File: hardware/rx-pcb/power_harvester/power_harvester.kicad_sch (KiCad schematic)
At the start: 47 parts, among them J1 Conn_Coaxial_Small, J2 Conn_01x02_Pin, J3 Conn_Coaxial_Small, J4 Conn_Coaxial_Small

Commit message: updates for dr weeks
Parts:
- C8: footprint (none) -> Capacitor_SMD:C_0805_2012Metric_Pad1.18x1.45mm_HandSolder
- J3, J4: footprint Connector_PinHeader_2.54mm:PinHeader_1x02_P2.54mm_Vertical -> Connector_Coaxial:SMA_Molex_73251-2120_EdgeMount_Horizontal
- L1, L3: footprint Inductor_SMD:L_0805_2012Metric_Pad1.05x1.20mm_HandSolder -> Inductor_SMD:L_0402_1005Metric
- R12, R13, R8: value off -> on
- R2: value on -> off
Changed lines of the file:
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@@
 			)
 		)
-		(property "Footprint" "Inductor_SMD:L_0805_2012Metric_Pad1.05x1.20mm_HandSolder"
+		(property "Footprint" "Inductor_SMD:L_0402_1005Metric"
 			(at 58.42 43.18 0)
 			(hide yes)
@@
 			)
 		)
-		(property "Value" "off"
+		(property "Value" "on"
 			(at 49.276 120.904 90)
 			(show_name no)
@@
 			)
 		)
-		(property "Footprint" ""
+		(property "Footprint" "Capacitor_SMD:C_0805_2012Metric_Pad1.18x1.45mm_HandSolder"
 			(at 164.1348 49.53 0)
 			(hide yes)
@@
 			)
 		)
-		(property "Footprint" "Inductor_SMD:L_0805_2012Metric_Pad1.05x1.20mm_HandSolder"
+		(property "Footprint" "Inductor_SMD:L_0402_1005Metric"
 			(at 58.42 48.26 0)
 			(hide yes)
@@
 			)
 		)
-		(property "Value" "off"
+		(property "Value" "on"
 			(at 63.246 120.904 90)
 			(show_name no)
@@
 			)
 		)
-		(property "Value" "on"
+		(property "Value" "off"
 			(at 68.326 120.904 90)
 			(show_name no)
@@
 			)
 		)
-		(property "Footprint" "Connector_PinHeader_2.54mm:PinHeader_1x02_P2.54mm_Vertical"
+		(property "Footprint" "Connector_Coaxial:SMA_Molex_73251-2120_EdgeMount_Horizontal"
 			(at 184.15 33.02 0)
 			(hide yes)
@@
 			)
 		)
-		(property "Footprint" "Connector_PinHeader_2.54mm:PinHeader_1x02_P2.54mm_Vertical"
+		(property "Footprint" "Connector_Coaxial:SMA_Molex_73251-2120_EdgeMount_Horizontal"
 			(at 123.19 33.02 0)
 			(hide yes)
@@
 			)
 		)
-		(property "Value" "off"
+		(property "Value" "on"
 			(at 65.786 120.904 90)
 			(show_name no)

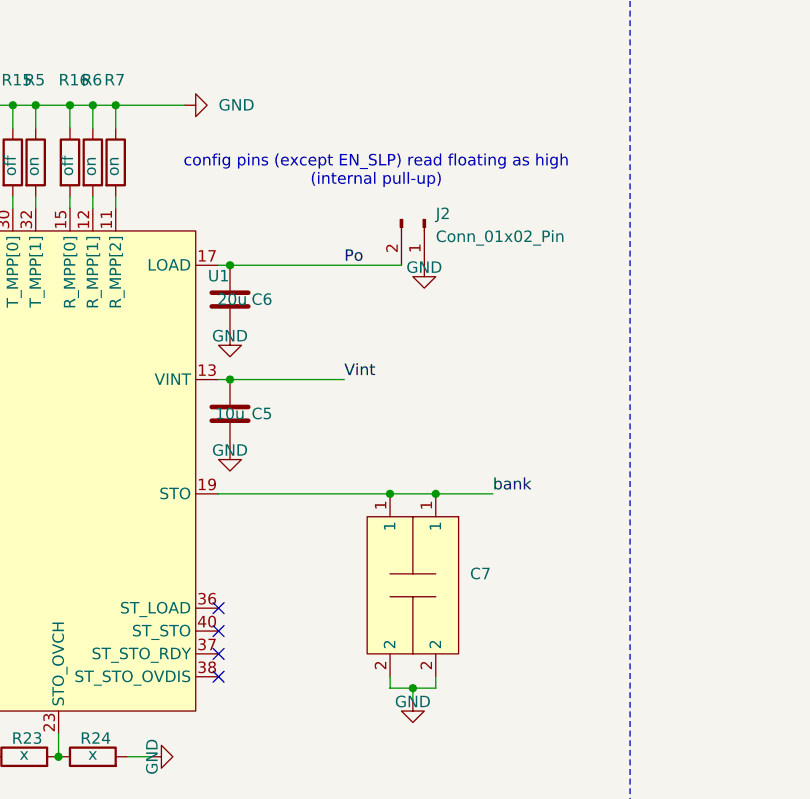
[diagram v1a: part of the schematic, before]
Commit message: updated PCB for weeks purchase
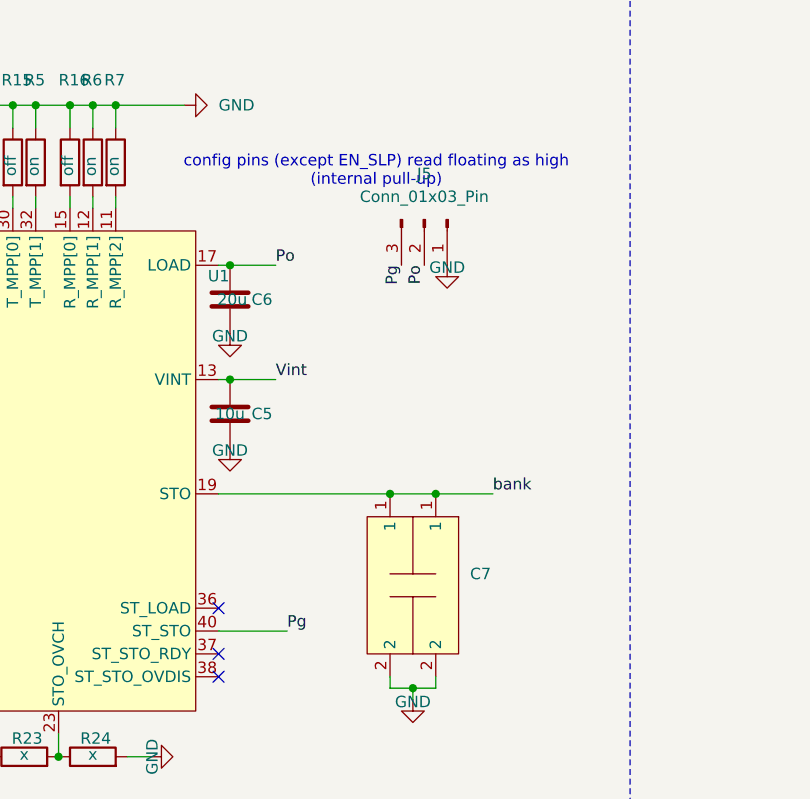
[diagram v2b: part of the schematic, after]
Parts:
- removed J2: Conn_01x02_Pin, Connector_PinHeader_2.54mm:PinHeader_1x02_P2.54mm_Vertical, symbol Connector:Conn_01x02_Pin
- added J5: Conn_01x03_Pin, Connector_PinHeader_2.54mm:PinHeader_1x03_P2.54mm_Vertical, symbol Connector:Conn_01x03_Pin
- D1, D2: footprint power_harvester:JDH2S02SL -> power_harvester:R_0201_0603Metric_correctedclearance
- D3, D4: footprint Capacitor_SMD:C_0201_0603Metric -> power_harvester:R_0201_0603Metric_correctedclearance
- R1, R10, R11, R12, R13, R14, R15, R16, R2, R3, R4, R5, R6, R7, R8, R9: footprint Resistor_SMD:R_0201_0603Metric -> power_harvester:R_0201_0603Metric_correctedclearance
- R17, R18, R19, R20: footprint Resistor_SMD:R_0201_0603Metric_Pad0.64x0.40mm_HandSolder -> power_harvester:R_0201_0603Metric_correctedclearance
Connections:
- net GND: now also J5.1 (Pin_1)
- net Po: now also J5.2 (Pin_2)
- net Pg: now reaches U1.40 (ST_STO)
- net Pg: now also J5.3 (Pin_3)
- no-connect marks 4 -> 3

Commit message: minor harvester updates
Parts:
- R12, R13, R4: value on -> off
- R14: value off -> on
- R21: value x -> 0
- R22: value x -> 19.5M
- R23: value x -> 100k
- R24: value x -> 5.6M
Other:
- note added: "R4 R3 R2 R1"
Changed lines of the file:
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@@
 		)
 	)
+	(text "R4     R3     R2     R1"
+		(exclude_from_sim no)
+		(at 78.74 188.468 0)
+		(effects
+			(font
+				(size 1.27 1.27)
+			)
+		)
+	)
 	(text "config pins (except EN_SLP) read floating as high\n(internal pull-up)"
 		(exclude_from_sim no)
@@
 			)
 		)
-		(property "Value" "x"
-			(at 75.438 185.166 90)
+		(property "Value" "19.5M"
+			(at 77.978 190.246 90)
 			(show_name no)
 			(do_not_autoplace no)
@@
 			)
 		)
-		(property "Value" "x"
-			(at 90.678 185.166 90)
+		(property "Value" "5.6M"
+			(at 91.948 190.246 90)
 			(show_name no)
 			(do_not_autoplace no)
@@
 			)
 		)
-		(property "Value" "x"
-			(at 83.058 185.166 90)
+		(property "Value" "100k"
+			(at 85.09 190.246 90)
 			(show_name no)
 			(do_not_autoplace no)
@@
 			)
 		)
-		(property "Value" "on"
+		(property "Value" "off"
 			(at 77.216 120.904 90)
 			(show_name no)
@@
 			)
 		)
-		(property "Value" "off"
+		(property "Value" "on"
 			(at 74.676 120.904 90)
 			(show_name no)
@@
 			)
 		)
-		(property "Value" "on"
+		(property "Value" "off"
 			(at 63.246 120.904 90)
 			(show_name no)
@@
 			)
 		)
-		(property "Value" "x"
-			(at 67.818 185.166 90)
+		(property "Value" "0"
+			(at 68.58 190.246 90)
 			(show_name no)
 			(do_not_autoplace no)
@@
 			)
 		)
-		(property "Value" "on"
+		(property "Value" "off"
 			(at 65.786 120.904 90)
 			(show_name no)

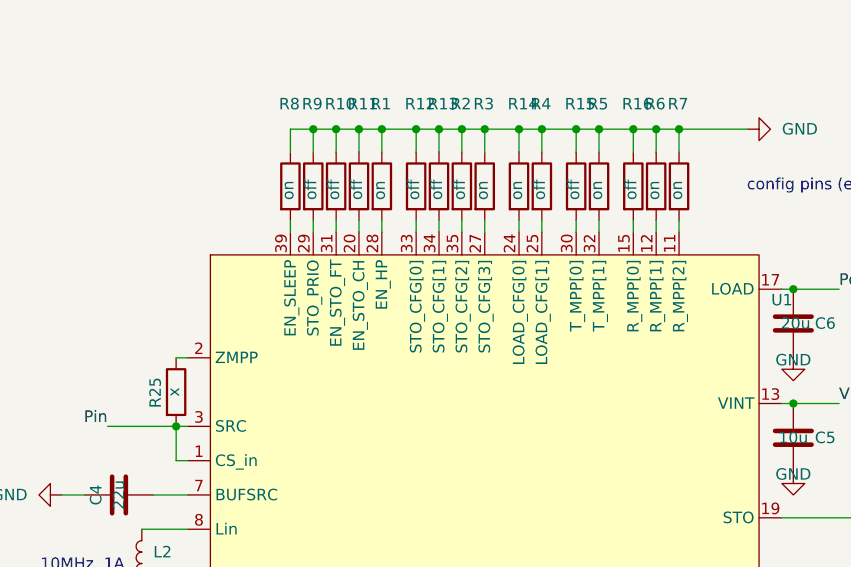
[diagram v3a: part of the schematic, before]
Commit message: updated power harvester hardware program
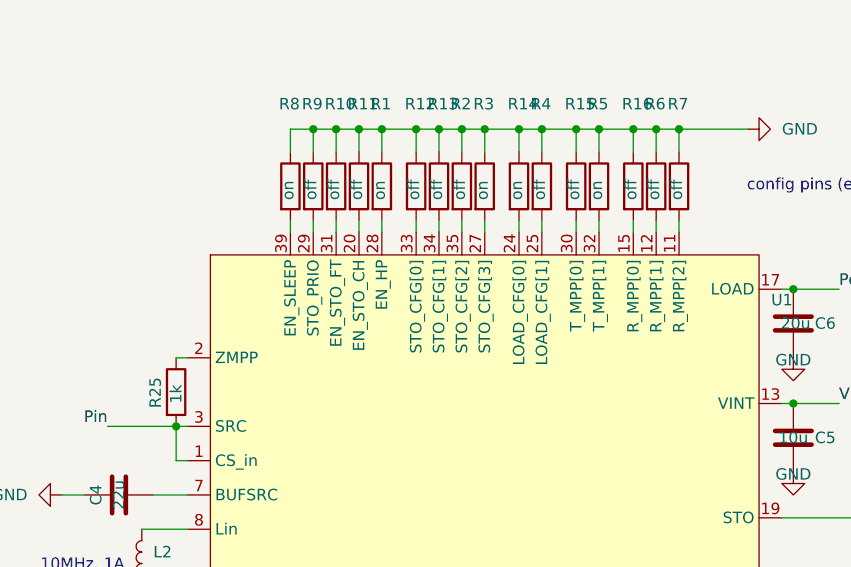
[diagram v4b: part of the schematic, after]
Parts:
- R25: value x -> 1k
- R6, R7: value on -> off
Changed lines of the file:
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@@
 			)
 		)
-		(property "Value" "on"
+		(property "Value" "off"
 			(at 92.456 120.904 90)
 			(show_name no)
@@
 			)
 		)
-		(property "Value" "x"
-			(at 36.576 142.748 90)
+		(property "Value" "1k"
+			(at 36.83 143.51 90)
 			(show_name no)
 			(do_not_autoplace no)
@@
 			)
 		)
-		(property "Value" "on"
+		(property "Value" "off"
 			(at 89.916 120.904 90)
 			(show_name no)
